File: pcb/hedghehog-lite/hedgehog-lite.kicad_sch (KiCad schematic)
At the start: 33 parts, among them J1 Conn_01x04, J2 AVR-ISP-6, SW1 Reset, SW2 SSSS811101, U1 ATmega32U4-M, Y1 16MHz

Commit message: Small PCB improvements
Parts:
- added JP2: HWB_EN, Jumper:SolderJumper-2_P1.3mm_Open_RoundedPad1.0x1.5mm, symbol Jumper:SolderJumper_2_Open
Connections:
- net at SW2.1, U1.33 (~{HWB}/PE2): now also JP2.1 (A)
- net at R2.2, SW2.2: now also JP2.2 (B)
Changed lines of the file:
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@@
   (junction (at 210.82 148.59) (diameter 0) (color 0 0 0 0)
   )
+  (junction (at 143.51 182.88) (diameter 0) (color 0 0 0 0)
+  )
   (junction (at 180.34 128.27) (diameter 0) (color 0 0 0 0)
   )
@@
   )
   (junction (at 210.82 128.27) (diameter 0) (color 0 0 0 0)
+  )
+  (junction (at 132.08 182.88) (diameter 0) (color 0 0 0 0)
   )
   (junction (at 210.82 113.03) (diameter 0) (color 0 0 0 0)
@@
     (stroke (width 0) (type default) (color 0 0 0 0))
   )
-  (wire (pts (xy 140.97 182.88) (xy 149.86 182.88))
+  (wire (pts (xy 140.97 182.88) (xy 143.51 182.88))
+    (stroke (width 0) (type default) (color 0 0 0 0))
+  )
+  (wire (pts (xy 143.51 182.88) (xy 149.86 182.88))
     (stroke (width 0) (type default) (color 0 0 0 0))
   )
@@
     (stroke (width 0) (type default) (color 0 0 0 0))
   )
+  (wire (pts (xy 143.51 186.055) (xy 143.51 182.88))
+    (stroke (width 0) (type default) (color 0 0 0 0))
+  )
   (wire (pts (xy 264.16 21.59) (xy 264.16 22.86))
     (stroke (width 0) (type default) (color 0 0 0 0))
@@
     (stroke (width 0) (type default) (color 0 0 0 0))
   )
+  (wire (pts (xy 132.08 186.055) (xy 132.08 182.88))
+    (stroke (width 0) (type default) (color 0 0 0 0))
+  )
   (wire (pts (xy 149.86 130.81) (xy 149.86 133.35))
     (stroke (width 0) (type default) (color 0 0 0 0))
@@
   )
   (wire (pts (xy 46.99 35.56) (xy 46.99 39.37))
+    (stroke (width 0) (type default) (color 0 0 0 0))
+  )
+  (wire (pts (xy 135.89 186.055) (xy 132.08 186.055))
     (stroke (width 0) (type default) (color 0 0 0 0))
   )
@@
     (pin "1")
   )
+  (symbol (lib_id "Jumper:SolderJumper_2_Open") (at 139.7 186.055 0) (unit 1)
+    (in_bom yes) (on_board yes)
+    (property "Reference" "JP2" (id 0) (at 139.7 188.595 0))
+    (property "Value" "HWB_EN" (id 1) (at 139.7 191.135 0))
+    (property "Footprint" "Jumper:SolderJumper-2_P1.3mm_Open_RoundedPad1.0x1.5mm" (id 2) (at 139.7 186.055 0)
+      (effects (font (size 1.27 1.27)) hide)
+    )
+    (property "Datasheet" "~" (id 3) (at 139.7 186.055 0)
+      (effects (font (size 1.27 1.27)) hide)
+    )
+    (pin "1")
+    (pin "2")
+  )
   (symbol (lib_id "bakeneko-60-pcb-rescue:GND-power") (at 26.67 43.18 0) (unit 1)
     (in_bom yes) (on_board yes)
@@
       (reference "JP1") (unit 1) (value "LED_PWR") (footprint "Jumper:SolderJumper-2_P1.3mm_Open_RoundedPad1.0x1.5mm")
     )
+    (path "/d5a06853-e99d-4a30-a3c9-add056fc1e69"
+      (reference "JP2") (unit 1) (value "HWB_EN") (footprint "Jumper:SolderJumper-2_P1.3mm_Open_RoundedPad1.0x1.5mm")
+    )
     (path "/eb09f9fb-b1c2-4630-9ea1-925f201f477f/b967e9d0-e03d-45ad-9ae1-1e09bcc9895d"

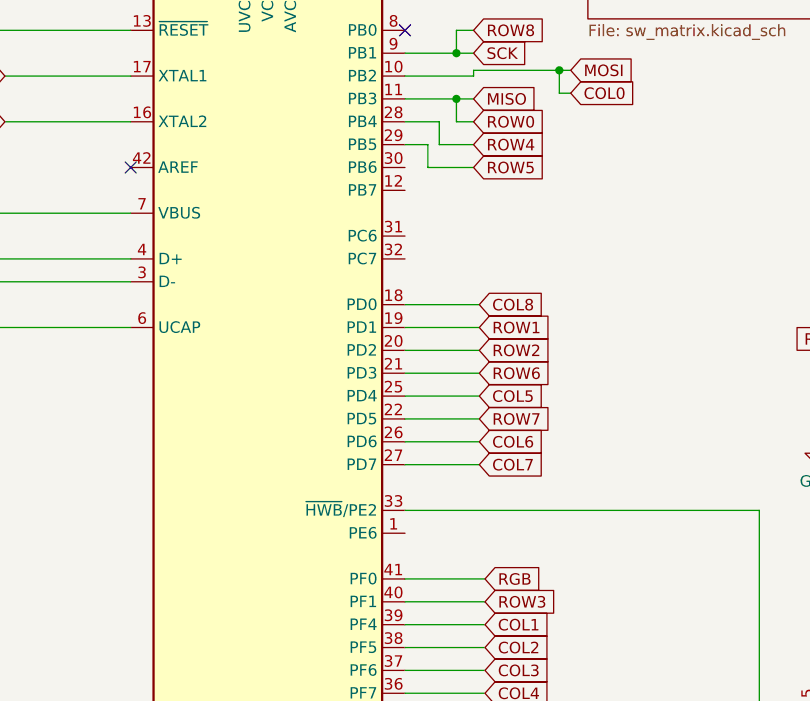
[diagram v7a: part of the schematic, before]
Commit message: Improved GND connection for atmega
This should not be needed but now all pins are connected to an external track
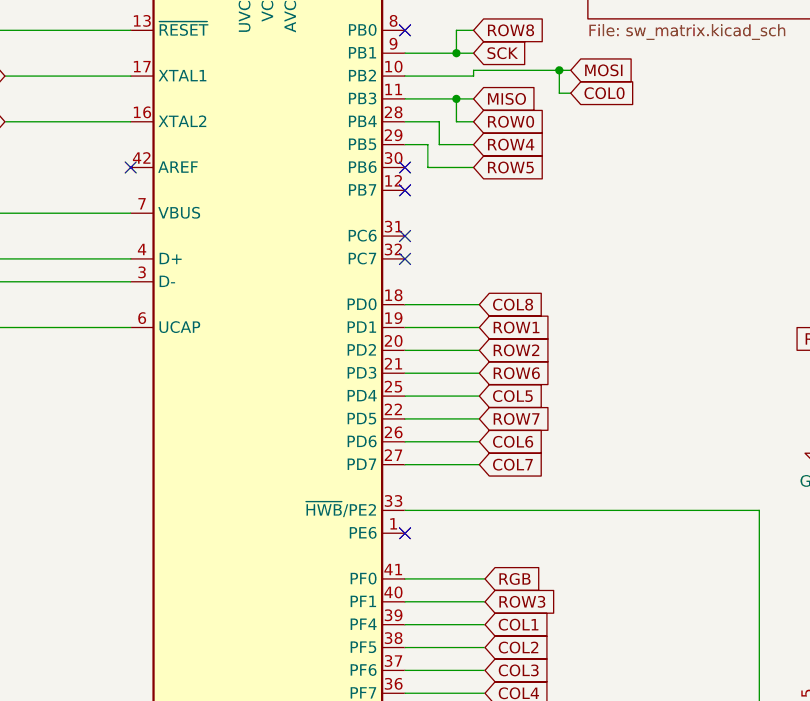
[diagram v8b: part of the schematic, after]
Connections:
- no-connect marks 8 -> 13
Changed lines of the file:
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@@
   (junction (at 77.47 73.66) (diameter 0) (color 0 0 0 0)
   )
+  (no_connect (at 92.71 104.14))
+  (no_connect (at 92.71 109.22))
+  (no_connect (at 92.71 111.76))
   (no_connect (at 92.71 86.36))
+  (no_connect (at 92.71 101.6))
   (no_connect (at 146.05 177.8))
   (no_connect (at 143.51 157.48))
   (no_connect (at 140.97 157.48))
+  (no_connect (at 92.71 142.24))
   (no_connect (at 143.51 177.8))
   (no_connect (at 62.23 101.6))
